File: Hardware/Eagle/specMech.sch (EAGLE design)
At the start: 86 parts, among them J1 PINHD-1X8-MOLEX-SHROUD, J2 MOLEX-22112022, J3 PINHD-1X8-MOLEX-SHROUD, J4 PINHD-1X8-MOLEX-SHROUD, J6 Molex 0022232081, J7 Lantronix XPORT, J8 Molex 0022232081, U1 MCP23008-E/SO, U10 ADS1115, U11 MCP23008-E/SO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

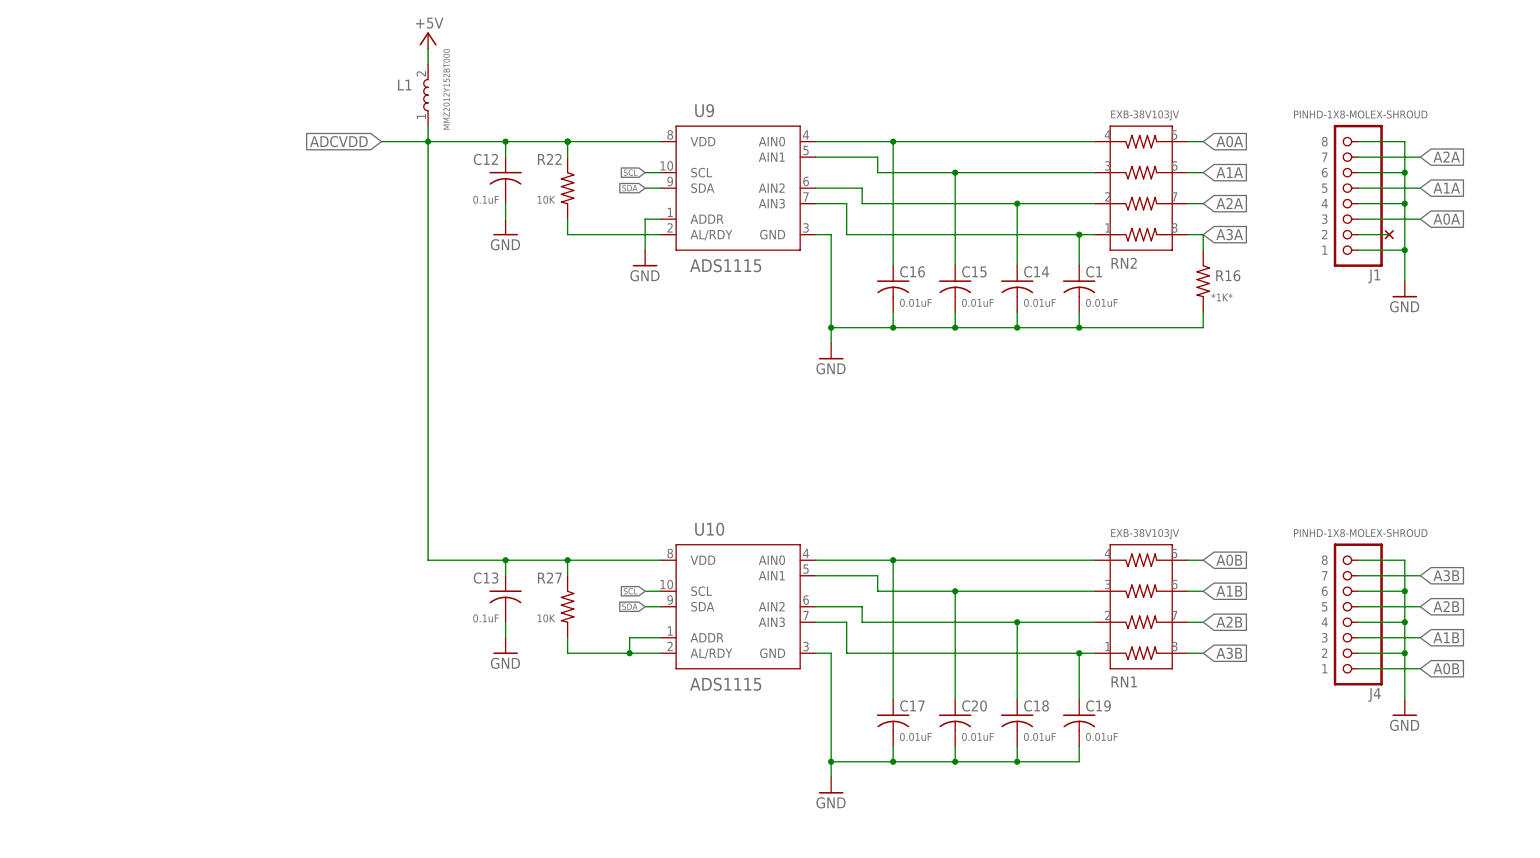
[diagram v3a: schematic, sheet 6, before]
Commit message: Added TVS diodes on ADC inputs
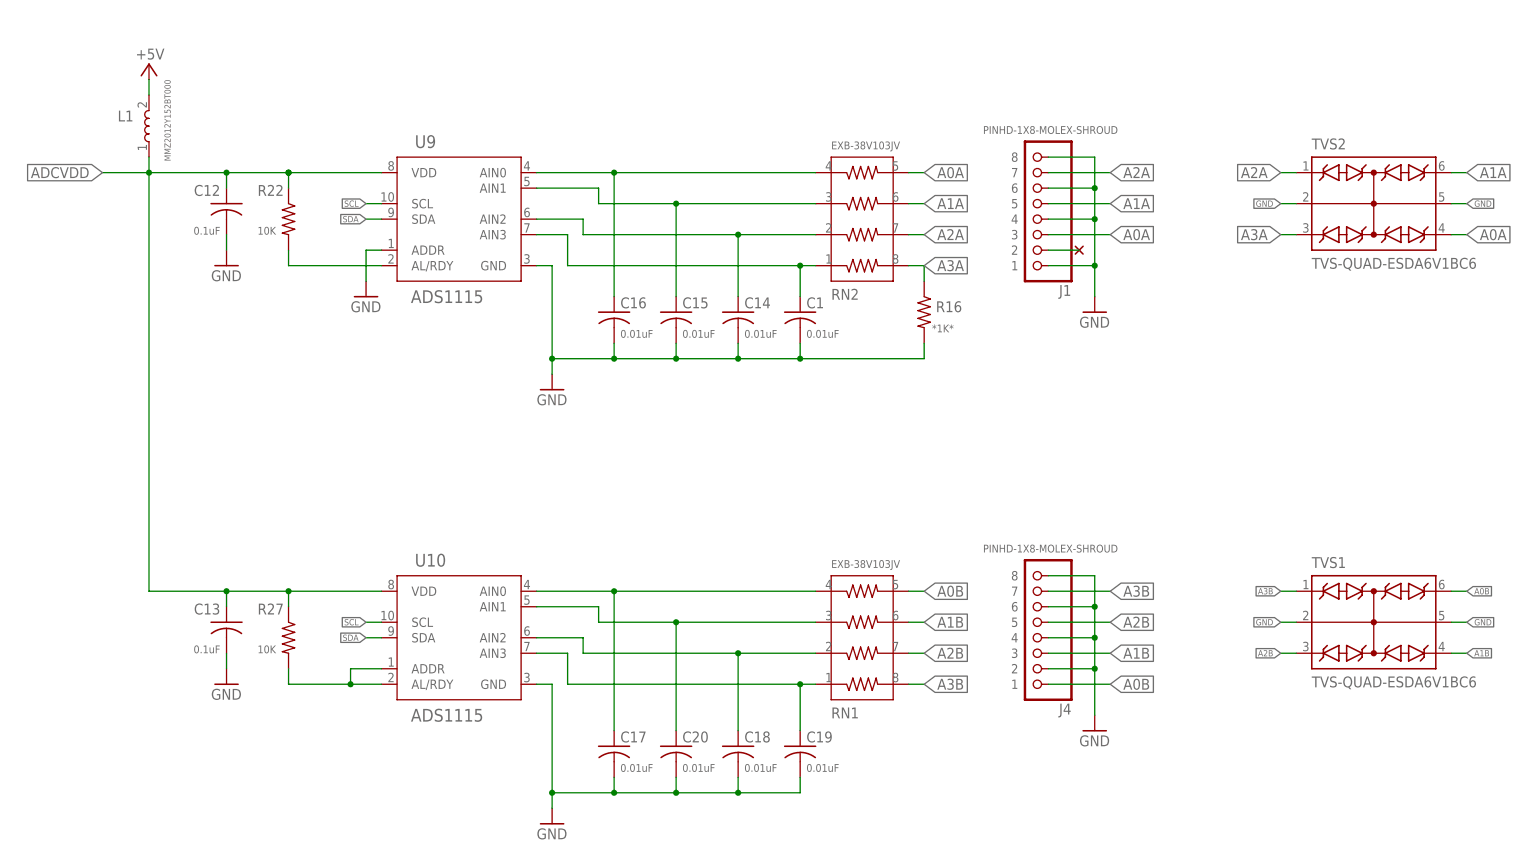
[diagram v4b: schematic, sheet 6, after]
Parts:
- added TVS1, TVS2: TVS-QUAD-ESDA6V1BC6, AUmlib:TVS-QUAD-ESDA6V1BC6
- U12: value 74HC2G17TSSOP-6 -> SCHMITT-TRIG-NC7WZ17P6X; device AUmlib:74HC2G17TSSOP-6 -> AUmlib:SCHMITT-TRIG-NC7WZ17P6X
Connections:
- net LN-RX renamed NANO-TX3
- net LN-TX renamed NANO-RX3
- net RX renamed NANO-RX1
- net TX renamed NANO-TX1
- removed net N$19: JP1.3, U12.1Y
- removed net N$8: JP1.7, U12.2A
- removed net RC-RX: CNANO1.PC0, U12.1A
- removed net RC-TX: CNANO1.PC1, U12.2Y
- new net COLL-RX: JP1.3, U12.Y1
- new net COLL-TX: JP1.7, U12.A2
- new net NANO-RX2: CNANO1.PC1, U12.Y2
- new net NANO-TX2: CNANO1.PC0, U12.A1
- net +5V: now also J2.2; no longer J2.1
- net A0A: now also TVS2.C3
- net A0B: now also TVS1.C4
- net A1A: now also TVS2.C4
- net A1B: now also TVS1.C3
- net A2A: now also TVS2.C1
- net A2B: now also TVS1.C2
- net A3A: now also TVS2.C2
- net A3B: now also TVS1.C1
- net GND: now also J2.1, TVS1.CC1, TVS1.CC2, TVS2.CC1, TVS2.CC2; no longer J2.2
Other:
- note removed: "Consider isoloator depending on roboclaw 12v handling"
- moved on the sheet: BO1, BT1, C1, C12, C13, C14, C15, C16, C17, C18, C19, C20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

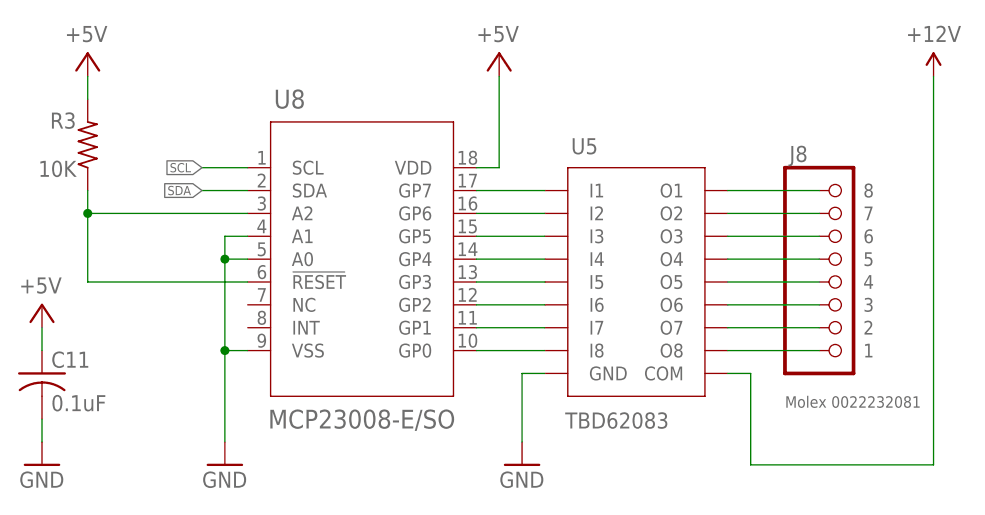
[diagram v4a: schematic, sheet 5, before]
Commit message: Updated part number for high current driver
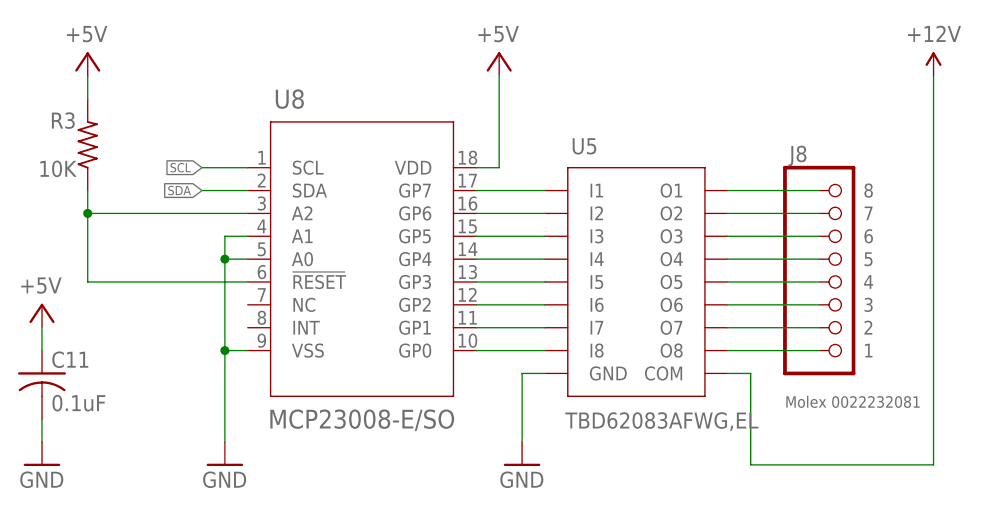
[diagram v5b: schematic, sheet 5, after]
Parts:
- U5: value TBD62083 -> TBD62083AFWG,EL
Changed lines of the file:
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@@
 <setting verticaltext="up"/>
 </settings>
-<grid distance="0.1" unitdist="inch" unit="inch" style="lines" multiple="1" display="yes" altdistance="0.01" altunitdist="inch" altunit="inch"/>
+<grid distance="0.1" unitdist="inch" unit="inch" style="lines" multiple="1" display="no" altdistance="0.01" altunitdist="inch" altunit="inch"/>
 <layers>
 <layer number="1" name="Top" color="4" fill="1" visible="no" active="no"/>
@@
 <part name="R14" library="AUmlib" library_urn="urn:adsk.eagle:library:9166017" deviceset="4609X-101-103LF" device="" package3d_urn="urn:adsk.eagle:package:15461702/6" value="10K"/>
 <part name="P+17" library="AUmlib" library_urn="urn:adsk.eagle:library:9166017" deviceset="+5V" device=""/>
-<part name="U5" library="AUmlib" library_urn="urn:adsk.eagle:library:9166017" deviceset="TBD62083" device="SOP18-P-375-1.27" package3d_urn="urn:adsk.eagle:package:10465865/2" value="TBD62083"/>
+<part name="U5" library="AUmlib" library_urn="urn:adsk.eagle:library:9166017" deviceset="TBD62083" device="SOP18-P-375-1.27" package3d_urn="urn:adsk.eagle:package:10465865/2" value="TBD62083AFWG,EL"/>
 <part name="U8" library="AUmlib" library_urn="urn:adsk.eagle:library:9166017" deviceset="MCP23008-E/SO" device="" package3d_urn="urn:adsk.eagle:package:18133672/2"/>
 <part name="P+19" library="AUmlib" library_urn="urn:adsk.eagle:library:9166017" deviceset="+5V" device=""/>

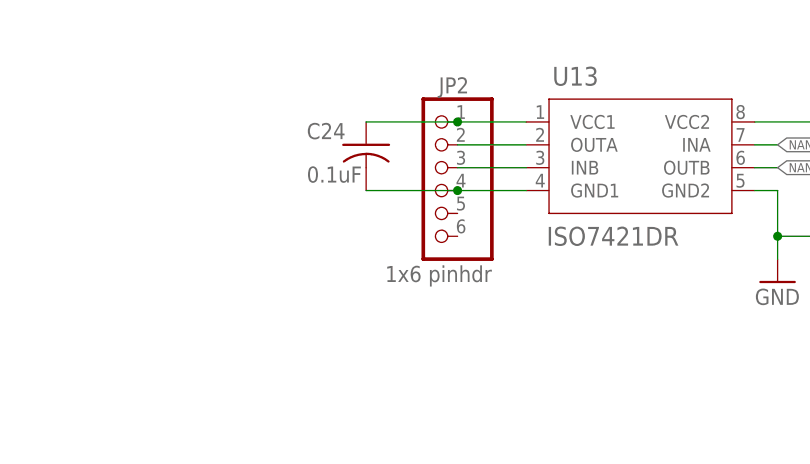
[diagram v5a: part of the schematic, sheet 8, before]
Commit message: Changed LN2 connector pinout to swap rx & tx
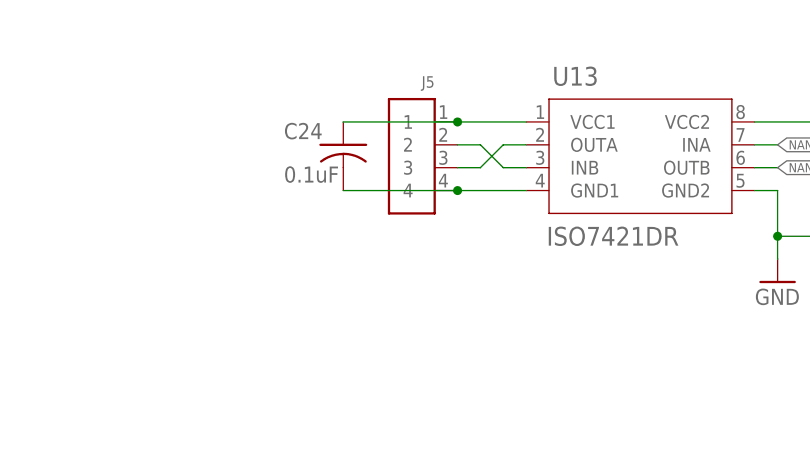
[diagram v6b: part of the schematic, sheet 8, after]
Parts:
- removed JP2: 1x6 pinhdr, AUmlib:PINHD-1X6
- added J5: (no value), AUmlib:PINHD-1X4-MOLEX-22112042
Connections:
- removed net GND1: C24.2, JP2.4, U13.GND1
- removed net N$26: JP2.3, U13.INB
- new net N$19: J5.3, U13.OUTA
- new net N$8: J5.2, U13.INB
- net N$23: now also J5.1; no longer JP2.1
- net N$25: now also C24.2, J5.4, U13.GND1; no longer JP2.2, U13.OUTA
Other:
- moved on the sheet: C24
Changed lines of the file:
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@@
 <setting verticaltext="up"/>
 </settings>
-<grid distance="0.1" unitdist="inch" unit="inch" style="lines" multiple="1" display="no" altdistance="0.01" altunitdist="inch" altunit="inch"/>
+<grid distance="0.1" unitdist="inch" unit="inch" style="lines" multiple="1" display="yes" altdistance="0.01" altunitdist="inch" altunit="inch"/>
 <layers>
 <layer number="1" name="Top" color="4" fill="1" visible="no" active="no"/>
@@
 <part name="SUPPLY10" library="AUmlib" library_urn="urn:adsk.eagle:library:9166017" deviceset="+12V" device=""/>
 <part name="U13" library="AUmlib" library_urn="urn:adsk.eagle:library:9166017" deviceset="ISO7421DR" device="TI-SOIC-D8" package3d_urn="urn:adsk.eagle:package:16444440/1" value="ISO7421DR"/>
-<part name="JP2" library="AUmlib" library_urn="urn:adsk.eagle:library:9166017" deviceset="PINHD-1X6" device="" package3d_urn="urn:adsk.eagle:package:24493396/1" value="1x6 pinhdr"/>
 <part name="C24" library="AUmlib" library_urn="urn:adsk.eagle:library:9166017" deviceset="C-US" device="C0805" package3d_urn="urn:adsk.eagle:package:4021265/3" value="0.1uF"/>
 <part name="C25" library="AUmlib" library_urn="urn:adsk.eagle:library:9166017" deviceset="C-US" device="C0805" package3d_urn="urn:adsk.eagle:package:4021265/3" value="0.1uF"/>
@@
 <part name="TVS1" library="AUmlib" library_urn="urn:adsk.eagle:library:9166017" deviceset="TVS-QUAD-ESDA6V1BC6" device="" package3d_urn="urn:adsk.eagle:package:25920714/2"/>
 <part name="TVS2" library="AUmlib" library_urn="urn:adsk.eagle:library:9166017" deviceset="TVS-QUAD-ESDA6V1BC6" device="" package3d_urn="urn:adsk.eagle:package:25920714/2"/>
+<part name="J5" library="AUmlib" library_urn="urn:adsk.eagle:library:9166017" deviceset="PINHD-1X4-MOLEX-22112042" device="" package3d_urn="urn:adsk.eagle:package:24729143/2"/>
 </parts>
 <sheets>
@@
 <attribute name="VALUE" x="218.1606" y="174.2186" size="2.0828" layer="96" rot="SR0"/>
 </instance>
-<instance part="JP2" gate="A" x="205.74" y="180.34" smashed="yes" rot="MR0">
-<attribute name="NAME" x="209.55" y="191.135" size="1.778" layer="95" rot="MR0"/>
-<attribute name="VALUE" x="212.09" y="170.18" size="1.778" layer="96" rot="MR0"/>
-</instance>
-<instance part="C24" gate="G$1" x="198.12" y="185.42" smashed="yes">
-<attribute name="NAME" x="191.516" y="186.055" size="1.778" layer="95"/>
-<attribute name="VALUE" x="191.516" y="181.229" size="1.778" layer="96"/>
+<instance part="C24" gate="G$1" x="195.58" y="185.42" smashed="yes">
+<attribute name="NAME" x="188.976" y="186.055" size="1.778" layer="95"/>
+<attribute name="VALUE" x="188.976" y="181.229" size="1.778" layer="96"/>
 </instance>
 <instance part="C25" gate="G$1" x="259.08" y="182.88" smashed="yes" rot="MR0">
@@
 <attribute name="VALUE" x="96.52" y="83.82" size="1.778" layer="96"/>
 </instance>
+<instance part="J5" gate="G$1" x="203.2" y="182.88" smashed="yes" rot="MR0">
+<attribute name="NAME" x="205.74" y="191.77" size="1.27" layer="95" rot="MR0"/>
+<attribute name="VALUE" x="205.74" y="175.26" size="1.27" layer="96" rot="MR0"/>
+</instance>
 </instances>
 <busses>
@@
 </segment>
 </net>
-<net name="N$23" class="0">
-<segment>
-<pinref part="JP2" gate="A" pin="1"/>
-<pinref part="U13" gate="G$1" pin="VCC1"/>
-<wire x1="208.28" y1="187.96" x2="215.9" y2="187.96" width="0.1524" layer="91"/>
-<pinref part="C24" gate="G$1" pin="1"/>
-<wire x1="198.12" y1="187.96" x2="208.28" y2="187.96" width="0.1524" layer="91"/>
-<junction x="208.28" y="187.96"/>
-</segment>
-</net>
-<net name="N$25" class="0">
-<segment>
-<pinref part="JP2" gate="A" pin="2"/>
-<pinref part="U13" gate="G$1" pin="OUTA"/>
-<wire x1="208.28" y1="185.42" x2="215.9" y2="185.42" width="0.1524" layer="91"/>
-</segment>
-</net>
-<net name="N$26" class="0">
-<segment>
-<pinref part="JP2" gate="A" pin="3"/>
-<pinref part="U13" gate="G$1" pin="INB"/>
-<wire x1="208.28" y1="182.88" x2="215.9" y2="182.88" width="0.1524" layer="91"/>
-</segment>
-</net>
-<net name="GND1" class="0">
-<segment>
-<pinref part="JP2" gate="A" pin="4"/>
-<pinref part="U13" gate="G$1" pin="GND1"/>
-<wire x1="208.28" y1="180.34" x2="215.9" y2="180.34" width="0.1524" layer="91"/>
-<pinref part="C24" gate="G$1" pin="2"/>
-<wire x1="198.12" y1="180.34" x2="208.28" y2="180.34" width="0.1524" layer="91"/>
-<junction x="208.28" y="180.34"/>
-</segment>
-</net>
 <net name="NANO-TX3" class="0">
 <segment>
@@
 </segment>
 </net>
+<net name="N$8" class="0">
+<segment>
+<pinref part="J5" gate="G$1" pin="2"/>
+<wire x1="208.28" y1="185.42" x2="210.82" y2="185.42" width="0.1524" layer="91"/>
+<wire x1="210.82" y1="185.42" x2="213.36" y2="182.88" width="0.1524" layer="91"/>
+<pinref part="U13" gate="G$1" pin="INB"/>
+<wire x1="213.36" y1="182.88" x2="215.9" y2="182.88" width="0.1524" layer="91"/>
+</segment>
+</net>
+<net name="N$19" class="0">
+<segment>
+<pinref part="J5" gate="G$1" pin="3"/>
+<wire x1="208.28" y1="182.88" x2="210.82" y2="182.88" width="0.1524" layer="91"/>
+<wire x1="210.82" y1="182.88" x2="213.36" y2="185.42" width="0.1524" layer="91"/>
+<pinref part="U13" gate="G$1" pin="OUTA"/>
+<wire x1="213.36" y1="185.42" x2="215.9" y2="185.42" width="0.1524" layer="91"/>
+</segment>
+</net>
+<net name="N$23" class="0">
+<segment>
+<pinref part="J5" gate="G$1" pin="1"/>
+<pinref part="U13" gate="G$1" pin="VCC1"/>
+<wire x1="208.28" y1="187.96" x2="215.9" y2="187.96" width="0.1524" layer="91"/>
+<pinref part="C24" gate="G$1" pin="1"/>
+<wire x1="195.58" y1="187.96" x2="208.28" y2="187.96" width="0.1524" layer="91"/>
+<junction x="208.28" y="187.96"/>
+</segment>
+</net>
+<net name="N$25" class="0">
+<segment>
+<pinref part="J5" gate="G$1" pin="4"/>
+<pinref part="U13" gate="G$1" pin="GND1"/>
+<wire x1="208.28" y1="180.34" x2="215.9" y2="180.34" width="0.1524" layer="91"/>
+<pinref part="C24" gate="G$1" pin="2"/>
+<wire x1="195.58" y1="180.34" x2="208.28" y2="180.34" width="0.1524" layer="91"/>
+<junction x="208.28" y="180.34"/>
+</segment>
+</net>
